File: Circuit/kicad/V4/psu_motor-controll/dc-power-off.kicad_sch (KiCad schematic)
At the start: 12 parts

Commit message: kicad psu pcb finish psu
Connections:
- net 12v_1: now also DC_U2.6 (IN); no longer DC_U1.6 (IN)
- net 12v_2: now also DC_U1.6 (IN); no longer DC_U2.6 (IN)
- net 3v3: now also DC_U5.6 (IN), DC_U6.6 (IN); no longer DC_U3.6 (IN), DC_U4.6 (IN)
- net 5v: now also DC_U3.6 (IN), DC_U4.6 (IN); no longer DC_U5.6 (IN), DC_U6.6 (IN)
- net B-B_2 renamed DC3.3V_2
- net B-B_3 renamed DC5V_2
- net B-B_4 renamed DC12V_2
- net B-B_5 renamed DC3.3V_1
- net B-B_6 renamed DC5V_1
- net B-B_7 renamed DC12V_1
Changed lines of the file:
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@@
 		)
 	)
-	(global_label "B-B_7"
+	(global_label "DC12V_1"
 		(shape input)
 		(at 86.36 67.31 180)
@@
 		)
 		(property "Intersheetrefs" "${INTERSHEET_REFS}"
-			(at 77.0853 67.31 0)
+			(at 75.055 67.31 0)
 			(effects
 				(font
@@
 		)
 	)
-	(global_label "B-B_5"
+	(global_label "DC5V_2"
+		(shape input)
+		(at 162.56 96.52 180)
+		(fields_autoplaced yes)
+		(effects
+			(font
+				(size 1.27 1.27)
+			)
+			(justify right)
+		)
+		(property "Intersheetrefs" "${INTERSHEET_REFS}"
+			(at 152.4645 96.52 0)
+			(effects
+				(font
+					(size 1.27 1.27)
+				)
+				(justify right)
+				(hide yes)
+			)
+		)
+	)
+	(global_label "DC3.3V_1"
 		(shape input)
 		(at 86.36 125.73 180)
@@
 		)
 		(property "Intersheetrefs" "${INTERSHEET_REFS}"
-			(at 77.0853 125.73 0)
+			(at 74.4502 125.73 0)
 			(effects
 				(font
@@
 		)
 	)
-	(global_label "B-B_6"
+	(global_label "DC12V_2"
+		(shape input)
+		(at 162.56 67.31 180)
+		(fields_autoplaced yes)
+		(effects
+			(font
+				(size 1.27 1.27)
+			)
+			(justify right)
+		)
+		(property "Intersheetrefs" "${INTERSHEET_REFS}"
+			(at 151.255 67.31 0)
+			(effects
+				(font
+					(size 1.27 1.27)
+				)
+				(justify right)
+				(hide yes)
+			)
+		)
+	)
+	(global_label "DC5V_1"
 		(shape input)
 		(at 86.36 96.52 180)
@@
 		)
 		(property "Intersheetrefs" "${INTERSHEET_REFS}"
-			(at 77.0853 96.52 0)
+			(at 76.2645 96.52 0)
 			(effects
 				(font
@@
 		)
 	)
-	(global_label "B-B_3"
-		(shape input)
-		(at 162.56 96.52 180)
-		(fields_autoplaced yes)
-		(effects
-			(font
-				(size 1.27 1.27)
-			)
-			(justify right)
-		)
-		(property "Intersheetrefs" "${INTERSHEET_REFS}"
-			(at 153.2853 96.52 0)
-			(effects
-				(font
-					(size 1.27 1.27)
-				)
-				(justify right)
-				(hide yes)
-			)
-		)
-	)
-	(global_label "B-B_2"
+	(global_label "DC3.3V_2"
 		(shape input)
 		(at 162.56 125.73 180)
@@
 		)
 		(property "Intersheetrefs" "${INTERSHEET_REFS}"
-			(at 153.2853 125.73 0)
-			(effects
-				(font
-					(size 1.27 1.27)
-				)
-				(justify right)
-				(hide yes)
-			)
-		)
-	)
-	(global_label "B-B_4"
-		(shape input)
-		(at 162.56 67.31 180)
-		(fields_autoplaced yes)
-		(effects
-			(font
-				(size 1.27 1.27)
-			)
-			(justify right)
-		)
-		(property "Intersheetrefs" "${INTERSHEET_REFS}"
-			(at 153.2853 67.31 0)
+			(at 150.6502 125.73 0)
 			(effects
 				(font
@@
 	(hierarchical_label "12v_2"
 		(shape input)
-		(at 162.56 59.69 180)
+		(at 86.36 59.69 180)
 		(effects
 			(font
@@
 	(hierarchical_label "5v"
 		(shape input)
-		(at 162.56 118.11 180)
+		(at 162.56 88.9 180)
 		(effects
 			(font
@@
 	(hierarchical_label "12v_1"
 		(shape input)
-		(at 86.36 59.69 180)
+		(at 162.56 59.69 180)
 		(effects
 			(font
@@
 	(hierarchical_label "3v3"
 		(shape input)
-		(at 86.36 88.9 180)
+		(at 86.36 118.11 180)
 		(effects
 			(font
@@
 	(hierarchical_label "5v"
 		(shape input)
-		(at 86.36 118.11 180)
+		(at 86.36 88.9 180)
 		(effects
 			(font
@@
 	(hierarchical_label "3v3"
 		(shape input)
-		(at 162.56 88.9 180)
+		(at 162.56 118.11 180)
 		(effects
 			(font

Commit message: PSU FINISH BOARD NO DRC,ERC,DFM ERRORS
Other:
- moved on the sheet: DC1, DC2, DC3, DC4, DC5, DC6, DC_U1, DC_U2, DC_U3, DC_U4, DC_U5, DC_U6

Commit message: V4.1.7 PSU  V1.0 debug Card
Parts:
- removed DC_U1, DC_U2: AP22815AWU, Package_TO_SOT_SMD:SOT-23-6, symbol Regulator_Linear:AP22615AWU
- added C21, C22: 68pf, Capacitor_SMD:C_0805_2012Metric, symbol Device:C
- added C23, C24: 1uf, Capacitor_SMD:C_0805_2012Metric, symbol Device:C
- added Q4, Q5: AO3400-CF, Package_TO_SOT_SMD:TSOT-23, symbol Simulation_SPICE:NMOS
- added R76, R78: 100r, Resistor_SMD:R_0805_2012Metric, symbol Device:R
- added R77, R79: 100k, Resistor_SMD:R_0805_2012Metric, symbol Device:R
- added U26, U27: MCP1401T-E, Package_TO_SOT_SMD:SOT-23-5, symbol Driver_FET:MCP1415
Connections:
- net 12v_1: now also C23.1, Q5.1 (D), U27.2 (Vdd)
- net 12v_2: now also C24.1, Q4.1 (D), U26.2 (Vdd)
- net DC12V_1: now also U27.3 (IN)
- net DC12V_2: now also U26.3 (IN)
- net GND: now also C21.2, C22.2, C23.2, C24.2, R77.2, R79.2, U26.4 (GND), U27.4 (GND)
- net at DC2.2 (Pin_2): now also Q5.3 (S)
- net at DC1.2 (Pin_2): now also Q4.3 (S)
- new net: C21.1, R78.2, R79.1, U27.5 (~{OUT})
- new net: C22.1, R76.2, R77.1, U26.5 (~{OUT})
- new net: Q5.2 (G), R78.1
- new net: Q4.2 (G), R76.1
- no-connect marks 12 -> 8
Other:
- moved on the sheet: DC1, DC2, DC3, DC4, DC5, DC6, DC_U3, DC_U4, DC_U5, DC_U6

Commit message: updated bom, updated compon
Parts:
- C21, C22: Cikkszám (none) -> 100.380.72; Link (none) -> https://www.hestore.hu/prod_10038072.html
- C23, C24: Cikkszám (none) -> 100.277.53; Link (none) -> https://www.hestore.hu/prod_10027753.html
- DC1, DC2, DC3, DC4, DC5, DC6: Cikkszám (none) -> 100.385.23; Link (none) -> https://www.hestore.hu/prod_10038523.html
- DC_U3, DC_U4, DC_U5, DC_U6: Cikkszám (none) -> 100.491.23; Link (none) -> https://www.hestore.hu/prod_10049123.html
- Q4, Q5: Cikkszám (none) -> 100.401.27; Link (none) -> https://www.hestore.hu/prod_10040127.html
- R76, R78: value 100r -> 100R; Cikkszám (none) -> 100.011.42; Link (none) -> https://www.hestore.hu/prod_10001142.html
- R77, R79: Cikkszám (none) -> 100.011.43; Link (none) -> https://www.hestore.hu/prod_10001143.html
- U26, U27: Cikkszám (none) -> 100.408.33; Link (none) -> https://www.hestore.hu/prod_10040833.html

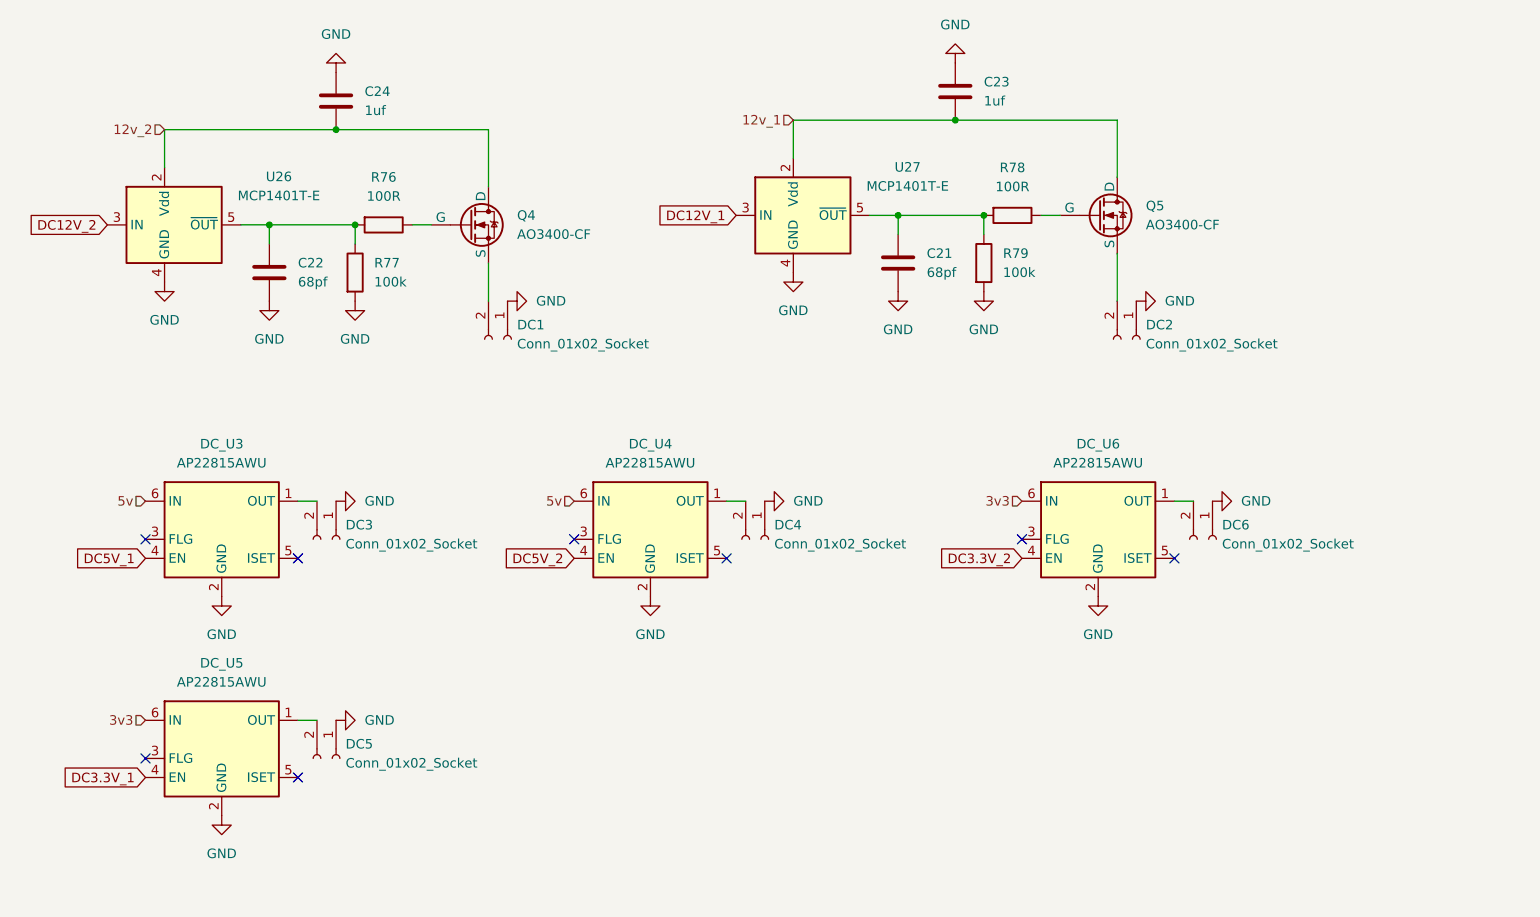
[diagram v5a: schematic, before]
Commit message: added psu start delay rc tag, high speed first inner and outboard impedance calculations
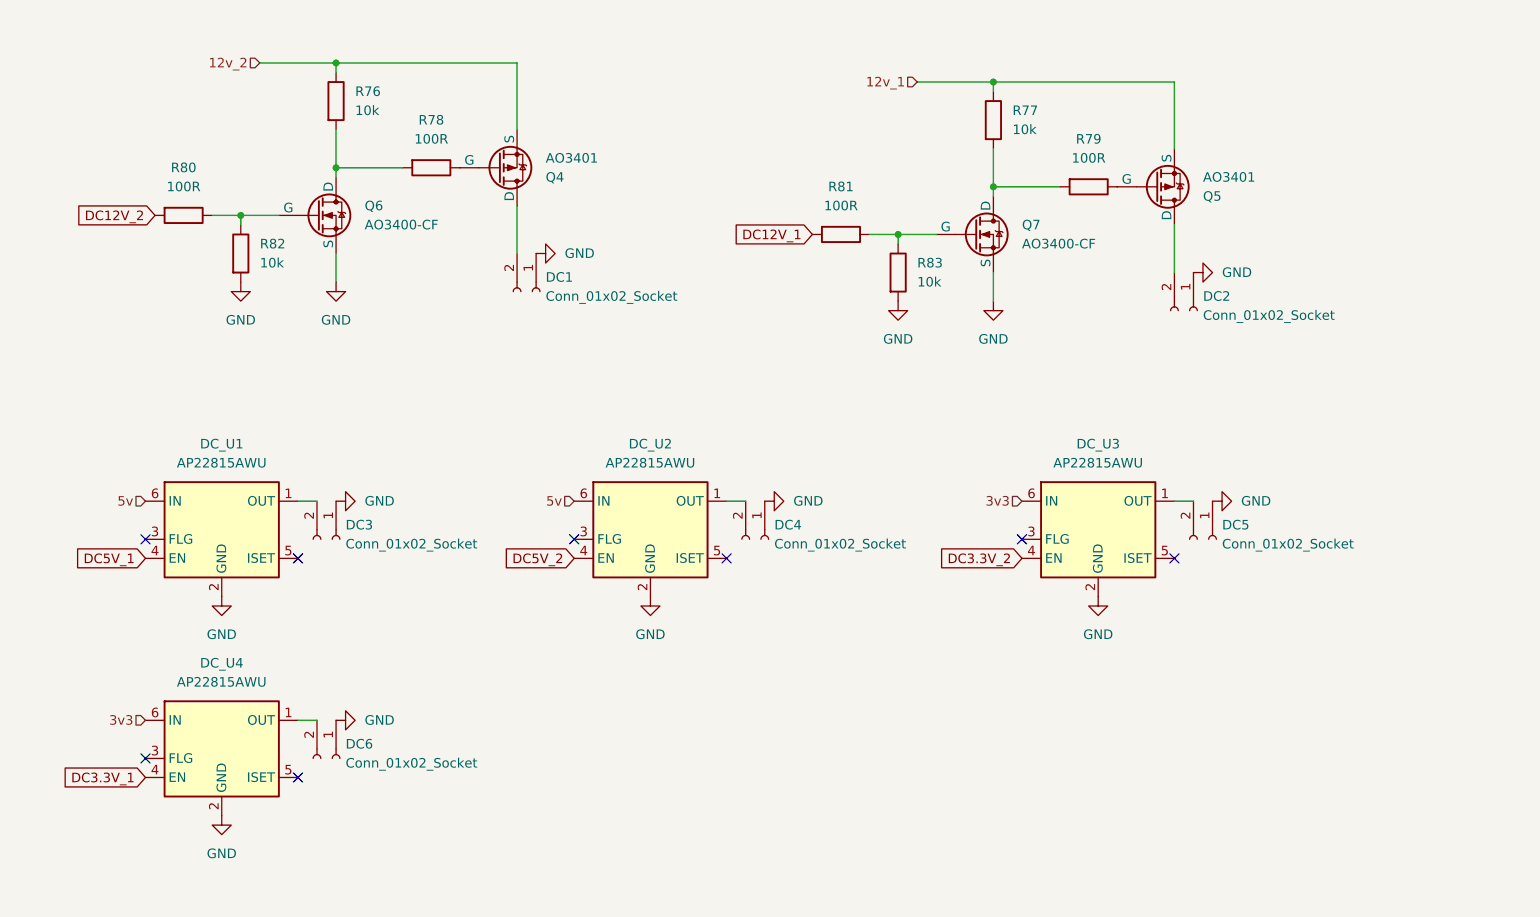
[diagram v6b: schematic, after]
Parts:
- removed C21, C22: 68pf, Capacitor_SMD:C_0805_2012Metric, symbol Device:C
- removed C23, C24: 1uf, Capacitor_SMD:C_0805_2012Metric, symbol Device:C
- removed Q4, Q5: AO3400-CF, Package_TO_SOT_SMD:TSOT-23, symbol Simulation_SPICE:NMOS
- removed U26, U27: MCP1401T-E, Package_TO_SOT_SMD:SOT-23-5, symbol Driver_FET:MCP1415
- added Q4, Q5: AO3401, Package_TO_SOT_SMD:TSOT-23, symbol Simulation_SPICE:PMOS
- added Q6, Q7: AO3400-CF, Package_TO_SOT_SMD:TSOT-23, symbol Simulation_SPICE:NMOS
- added R76, R82, R83: 10k, Resistor_SMD:R_0805_2012Metric, symbol Device:R
- added R81: 100R, Resistor_SMD:R_0805_2012Metric, symbol Device:R
- R77: value 100k -> 10k
- R79: value 100k -> 100R; Cikkszám 100.011.43 -> 100.011.42; Link https://www.hestore.hu/prod_10001143.html -> https://www.hestore.hu/prod_10001142.html
- renumbered DC6 to DC5, DC5 to DC6, DC_U3 to DC_U1, DC_U4 to DC_U2, DC_U6 to DC_U3, DC_U5 to DC_U4, R76 to R80
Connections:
- net 12v_1: now also R77.1, Q5.3 (S)
- net 12v_2: now also Q4.3 (S), R76.1
- net DC12V_1: now also R81.2
- net DC12V_2: now also R80.2
- net GND: now also Q6.3 (S), Q7.3 (S), R82.2, R83.2; no longer R77.2, R79.2
- net at R78.2: now also Q6.1 (D), R76.2; no longer R79.1
- net at DC2.2 (Pin_2): now also Q5.1 (D)
- net at R78.1: now also Q4.2 (G)
- net at R80.1: now also Q6.2 (G), R82.1
- net at DC1.2 (Pin_2): now also Q4.1 (D)
- new net: Q7.2 (G), R81.1, R83.1
- new net: Q7.1 (D), R77.2, R79.2
- new net: Q5.2 (G), R79.1
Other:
- moved on the sheet: R80

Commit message: kicad update
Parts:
- Q4, Q5: Cikkszám (none) -> 100.401.26; Link (none) -> https://www.hestore.hu/prod_10040126.html
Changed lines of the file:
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@@
+			)
+		)
+		(property "Cikkszám" "100.401.26"
+			(at 78.74 39.37 0)
+			(effects
+				(font
+					(size 1.27 1.27)
+				)
+				(hide yes)
+			)
+		)
+		(property "Link" "https://www.hestore.hu/prod_10040126.html"
+			(at 78.74 39.37 0)
+			(effects
+				(font
+					(size 1.27 1.27)
+				)
+				(hide yes)
 			)
 		)
@@
 			(effects
 				(font
+					(size 1.27 1.27)
+				)
+				(hide yes)
+			)
+		)
+		(property "Cikkszám" "100.401.26"
+			(at 166.37 41.91 0)
+			(effects
+				(font
+					(size 1.27 1.27)
+				)
+				(hide yes)
+			)
+		)
+		(property "Link" "https://www.hestore.hu/prod_10040126.html"
+			(at 166.37 41.91 0)
+			(effects
+				(font

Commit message: FINISH PSU V1.4.9 to production 1
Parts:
- DC_U1, DC_U2, DC_U3, DC_U4: footprint Package_TO_SOT_SMD:SOT-23-6 -> panel:TSOT-26
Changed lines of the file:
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@@
 			)
 		)
-		(property "Footprint" "Package_TO_SOT_SMD:SOT-23-6"
+		(property "Footprint" "panel:TSOT-26"
 			(at 41.91 105.41 0)
 			(effects
@@
 			)
 		)
-		(property "Footprint" "Package_TO_SOT_SMD:SOT-23-6"
+		(property "Footprint" "panel:TSOT-26"
 			(at 99.06 105.41 0)
 			(effects
@@
 			)
 		)
-		(property "Footprint" "Package_TO_SOT_SMD:SOT-23-6"
+		(property "Footprint" "panel:TSOT-26"
 			(at 158.75 105.41 0)
 			(effects
@@
 			)
 		)
-		(property "Footprint" "Package_TO_SOT_SMD:SOT-23-6"
+		(property "Footprint" "panel:TSOT-26"
 			(at 41.91 134.62 0)
 			(effects
